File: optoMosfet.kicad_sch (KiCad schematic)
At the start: 0 parts

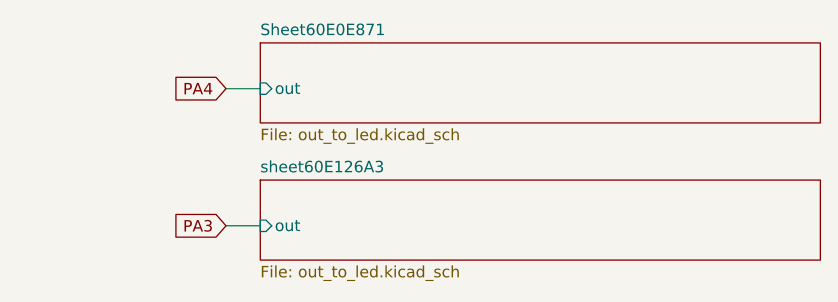
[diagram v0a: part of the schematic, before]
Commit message: Planteamiento nuevo proeycto de mosquito - Se eelmiraon del esquematico las entradas a 0V y las salidas a Leds
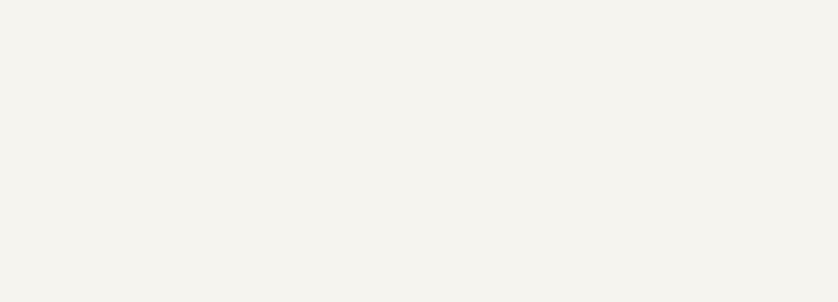
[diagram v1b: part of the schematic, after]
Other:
- removed sheet Sheet60E0E871
- removed sheet sheet60E126A3
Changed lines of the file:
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@@
-    (stroke (width 0) (type default))
-  )
-  (wire (pts (xy 166.37 27.94) (xy 170.18 27.94))
-    (stroke (width 0) (type default))
-  )
-  (wire (pts (xy 166.37 43.18) (xy 170.18 43.18))
     (stroke (width 0) (type default))
   )
@@
     (effects (font (size 1.27 1.27)) (justify right))
     (property "Intersheetrefs" "${INTERSHEET_REFS}" (at 21.59 41.91 0)
-      (effects (font (size 1.27 1.27)) hide)
-    )
-  )
-  (global_label "PA3" (shape input) (at 166.37 43.18 180)
-    (effects (font (size 1.27 1.27)) (justify right))
-    (property "Intersheetrefs" "${INTERSHEET_REFS}" (at 166.37 43.18 0)
-      (effects (font (size 1.27 1.27)) hide)
-    )
-  )
-  (global_label "PA4" (shape input) (at 166.37 27.94 180)
-    (effects (font (size 1.27 1.27)) (justify right))
-    (property "Intersheetrefs" "${INTERSHEET_REFS}" (at 166.37 27.94 0)
       (effects (font (size 1.27 1.27)) hide)
     )
@@
       )
     )
-  )
-  (sheet (at 170.18 22.86) (size 62.23 8.89) (fields_autoplaced)
-    (stroke (width 0) (type solid))
-    (fill (color 0 0 0 0.0000))
-    (property "Sheetname" "Sheet60E0E871" (at 170.18 22.1484 0)
-      (effects (font (size 1.27 1.27)) (justify left bottom))
-    )
-    (property "Sheetfile" "out_to_led.kicad_sch" (at 170.18 32.3346 0)
-      (effects (font (size 1.27 1.27)) (justify left top))
-    )
-    (pin "out" input (at 170.18 27.94 180)
-      (effects (font (size 1.27 1.27)) (justify left))
-    )
-    (instances
-      (project "jac_board"
-        (path "/b4f2a1b7-be95-447b-917e-345a5a8cb173/00000000-0000-0000-0000-000060cc612c" (page "5"))
-      )
-    )
-  )
-  (sheet (at 170.18 38.1) (size 62.23 8.89) (fields_autoplaced)
-    (stroke (width 0) (type solid))
-    (fill (color 0 0 0 0.0000))
-    (property "Sheetname" "sheet60E126A3" (at 170.18 37.3884 0)
-      (effects (font (size 1.27 1.27)) (justify left bottom))
-    )
-    (property "Sheetfile" "out_to_led.kicad_sch" (at 170.18 47.5746 0)
-      (effects (font (size 1.27 1.27)) (justify left top))
-    )
-    (pin "out" input (at 170.18 43.18 180)
-      (effects (font (size 1.27 1.27)) (justify left))
-    )
-    (instances
-      (project "jac_board"
-        (path "/b4f2a1b7-be95-447b-917e-345a5a8cb173/00000000-0000-0000-0000-000060cc612c" (page "6"))
-      )
-    )
